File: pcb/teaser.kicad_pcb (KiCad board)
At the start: 2 copper layers, 43 x 115 mm, 69 parts, among them J1 Programator, J2 AC_Plug, J3 OLED, J4 battery, Q1 MMBTA44, Q2 MMBTA44, Q3 MMBTA44, Q4 MMBTA44, Q6 AO3401A, SW1 Włancznik, SW7 SW_Push, U2 LM1117MP-5.0, U3 ATmega328P-A, Y1 16kHz

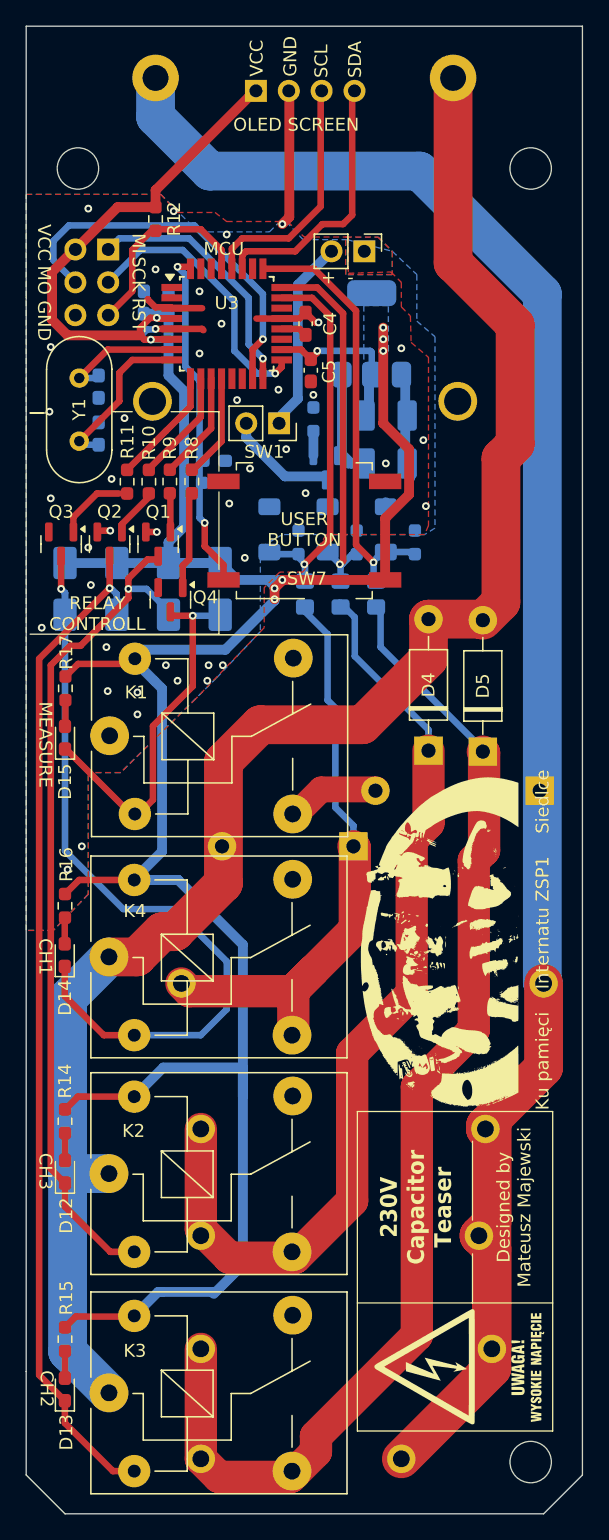
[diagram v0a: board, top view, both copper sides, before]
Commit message: Updated board outline and regenerated gerbers
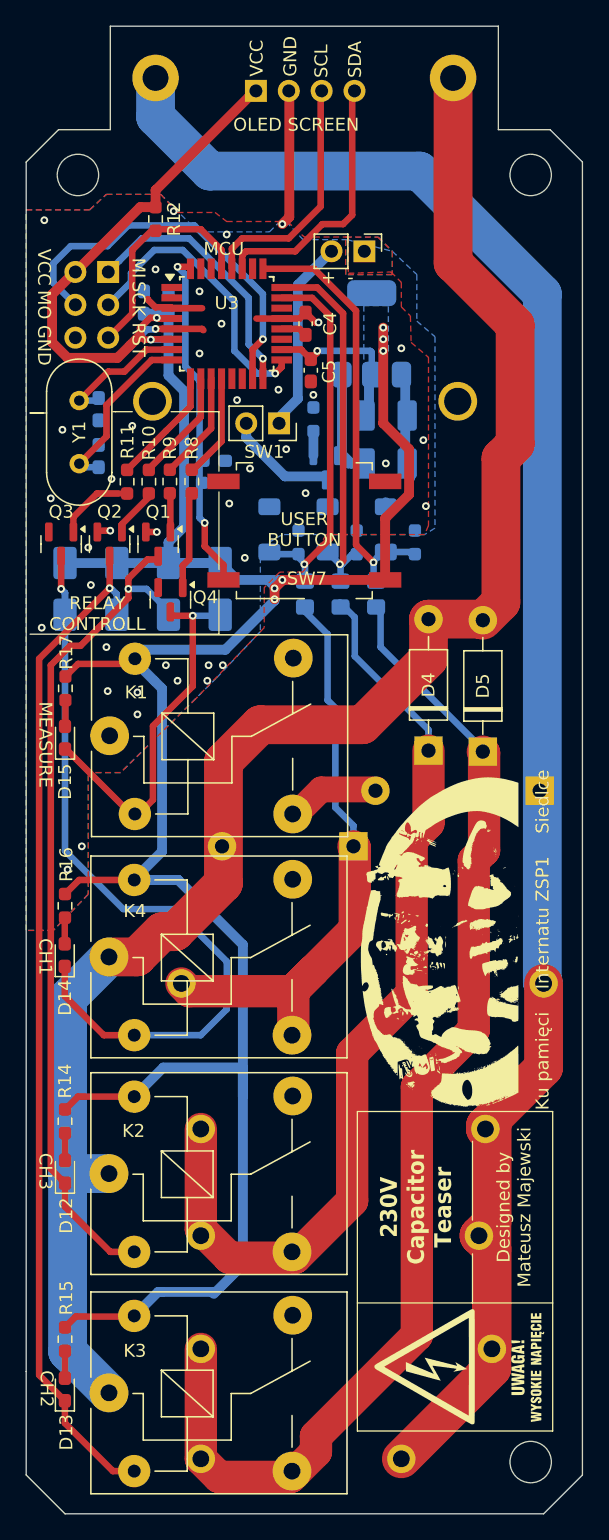
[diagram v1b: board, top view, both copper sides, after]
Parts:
- moved J1 1.74 mm to (127.3, 62.5)
- moved C13 1.74 mm to (126.6, 73.1)
- moved C14 1.74 mm to (126.6, 76.7)
- moved Y1 1.74 mm to (125.1, 77.3)
- moved H1 0.50 mm to (125.0, 55.0)
- moved H2 0.50 mm to (160.0, 55.0)
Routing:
- net /RESET: track 15.5 -> 17.2 mm
- net VCC: track 247.7 -> 249.2 mm
- net /SCK: track 21.4 -> 22.5 mm
- net Net-(U3-XTAL2/PB7): track 12.8 -> 13.6 mm
- net /MOSI: track 29.8 -> 30.5 mm
- net /MISO: track 19.8 -> 20.5 mm
- net Net-(U3-XTAL1/PB6): track 10.2 -> 10.9 mm
- net GND: vias 43 -> 42
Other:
- outline, holes or cut-outs redrawn
